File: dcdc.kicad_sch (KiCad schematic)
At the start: 25 parts, among them J10 Conn_01x01, J8 Conn_01x01, J9 Conn_01x01, T1 Transformer_SP_1S, U1 L78L33_SOT89, U2 TMP117, U3 LT3439

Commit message: asdf
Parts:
- added J11, J12: Conn_01x01, Connector_Wire:SolderWire-1sqmm_1x01_D1.4mm_OD3.9mm, symbol Connector_Generic:Conn_01x01
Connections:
- net 0Vout: now also J12.1 (Pin_1)
- net 12Vout: now also J11.1 (Pin_1)
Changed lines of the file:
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@@
+    (stroke (width 0) (type default) (color 0 0 0 0))
+  )
+  (wire (pts (xy 227.33 69.85) (xy 190.5 69.85))
     (stroke (width 0) (type default) (color 0 0 0 0))
   )
@@
     (stroke (width 0) (type default) (color 0 0 0 0))
   )
+  (wire (pts (xy 229.87 82.55) (xy 190.5 82.55))
+    (stroke (width 0) (type default) (color 0 0 0 0))
+  )
+  (wire (pts (xy 190.5 69.85) (xy 190.5 66.04))
+    (stroke (width 0) (type default) (color 0 0 0 0))
+  )
   (wire (pts (xy 116.84 101.6) (xy 127 101.6))
     (stroke (width 0) (type default) (color 0 0 0 0))
@@
   )
   (wire (pts (xy 49.53 134.62) (xy 49.53 137.16))
+    (stroke (width 0) (type default) (color 0 0 0 0))
+  )
+  (wire (pts (xy 190.5 82.55) (xy 190.5 74.93))
     (stroke (width 0) (type default) (color 0 0 0 0))
   )
@@
     (pin "1")
   )
+  (symbol (lib_id "Connector_Generic:Conn_01x01") (at 185.42 66.04 0) (mirror y) (unit 1)
+    (in_bom yes) (on_board yes) (fields_autoplaced)
+    (property "Reference" "J11" (id 0) (at 185.42 59.69 0))
+    (property "Value" "Conn_01x01" (id 1) (at 185.42 62.23 0))
+    (property "Footprint" "Connector_Wire:SolderWire-1sqmm_1x01_D1.4mm_OD3.9mm" (id 2) (at 185.42 66.04 0)
+      (effects (font (size 1.27 1.27)) hide)
+    )
+    (property "Datasheet" "~" (id 3) (at 185.42 66.04 0)
+      (effects (font (size 1.27 1.27)) hide)
+    )
+    (pin "1")
+  )
   (symbol (lib_id "Device:R") (at 59.69 140.97 0) (unit 1)
     (in_bom yes) (on_board yes) (fields_autoplaced)
@@
     (pin "2")
   )
+  (symbol (lib_id "Connector_Generic:Conn_01x01") (at 185.42 74.93 0) (mirror y) (unit 1)
+    (in_bom yes) (on_board yes) (fields_autoplaced)
+    (property "Reference" "J12" (id 0) (at 185.42 68.58 0))
+    (property "Value" "Conn_01x01" (id 1) (at 185.42 71.12 0))
+    (property "Footprint" "Connector_Wire:SolderWire-1sqmm_1x01_D1.4mm_OD3.9mm" (id 2) (at 185.42 74.93 0)
+      (effects (font (size 1.27 1.27)) hide)
+    )
+    (property "Datasheet" "~" (id 3) (at 185.42 74.93 0)
+      (effects (font (size 1.27 1.27)) hide)
+    )
+    (pin "1")
+  )
   (symbol (lib_id "Regulator_Switching:LT3439") (at 129.54 78.74 0) (unit 1)

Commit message: asdf
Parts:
- added H1, H2, H3, H4, H5, H6, H7, H8: MountingHole, MountingHole:MountingHole_4.3mm_M4, symbol Mechanical:MountingHole
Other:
- moved on the sheet: D1
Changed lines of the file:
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@@
     (pin "2")
+  )
+  (symbol (lib_id "Mechanical:MountingHole") (at 165.1 27.94 0) (unit 1)
+    (in_bom yes) (on_board yes) (fields_autoplaced)
+    (property "Reference" "H2" (id 0) (at 162.56 26.6699 0)
+      (effects (font (size 1.27 1.27)) (justify right))
+    )
+    (property "Value" "MountingHole" (id 1) (at 162.56 29.2099 0)
+      (effects (font (size 1.27 1.27)) (justify right))
+    )
+    (property "Footprint" "MountingHole:MountingHole_4.3mm_M4" (id 2) (at 165.1 27.94 0)
+      (effects (font (size 1.27 1.27)) hide)
+    )
+    (property "Datasheet" "~" (id 3) (at 165.1 27.94 0)
+      (effects (font (size 1.27 1.27)) hide)
+    )
   )
   (symbol (lib_id "power:GND") (at 77.47 180.34 0) (unit 1)
@@
     (pin "1")
     (pin "2")
+  )
+  (symbol (lib_id "Mechanical:MountingHole") (at 171.45 22.86 0) (unit 1)
+    (in_bom yes) (on_board yes) (fields_autoplaced)
+    (property "Reference" "H5" (id 0) (at 173.99 21.5899 0)
+      (effects (font (size 1.27 1.27)) (justify left))
+    )
+    (property "Value" "MountingHole" (id 1) (at 173.99 24.1299 0)
+      (effects (font (size 1.27 1.27)) (justify left))
+    )
+    (property "Footprint" "MountingHole:MountingHole_4.3mm_M4" (id 2) (at 171.45 22.86 0)
+      (effects (font (size 1.27 1.27)) hide)
+    )
+    (property "Datasheet" "~" (id 3) (at 171.45 22.86 0)
+      (effects (font (size 1.27 1.27)) hide)
+    )
   )
   (symbol (lib_id "Connector_Generic:Conn_01x01") (at 185.42 74.93 0) (mirror y) (unit 1)
@@
     (pin "2")
   )
+  (symbol (lib_id "Mechanical:MountingHole") (at 165.1 22.86 0) (unit 1)
+    (in_bom yes) (on_board yes) (fields_autoplaced)
+    (property "Reference" "H1" (id 0) (at 162.56 21.5899 0)
+      (effects (font (size 1.27 1.27)) (justify right))
+    )
+    (property "Value" "MountingHole" (id 1) (at 162.56 24.1299 0)
+      (effects (font (size 1.27 1.27)) (justify right))
+    )
+    (property "Footprint" "MountingHole:MountingHole_4.3mm_M4" (id 2) (at 165.1 22.86 0)
+      (effects (font (size 1.27 1.27)) hide)
+    )
+    (property "Datasheet" "~" (id 3) (at 165.1 22.86 0)
+      (effects (font (size 1.27 1.27)) hide)
+    )
+  )
   (symbol (lib_id "Regulator_Linear:L78L33_SOT89") (at 45.72 102.87 0) (unit 1)
     (in_bom yes) (on_board yes) (fields_autoplaced)
@@
     (pin "1")
   )
-  (symbol (lib_id "Device:LED") (at 233.68 36.83 180) (unit 1)
-    (in_bom yes) (on_board yes) (fields_autoplaced)
-    (property "Reference" "D1" (id 0) (at 235.2675 29.21 0))
-    (property "Value" "LED" (id 1) (at 235.2675 31.75 0))
-    (property "Footprint" "LED_SMD:LED_1206_3216Metric" (id 2) (at 233.68 36.83 0)
-      (effects (font (size 1.27 1.27)) hide)
-    )
-    (property "Datasheet" "~" (id 3) (at 233.68 36.83 0)
+  (symbol (lib_id "Device:LED") (at 233.68 31.75 180) (unit 1)
+    (in_bom yes) (on_board yes) (fields_autoplaced)
+    (property "Reference" "D1" (id 0) (at 235.2675 24.13 0))
+    (property "Value" "LED" (id 1) (at 235.2675 26.67 0))
+    (property "Footprint" "LED_SMD:LED_1206_3216Metric" (id 2) (at 233.68 31.75 0)
+      (effects (font (size 1.27 1.27)) hide)
+    )
+    (property "Datasheet" "~" (id 3) (at 233.68 31.75 0)
       (effects (font (size 1.27 1.27)) hide)
     )
@@
     (pin "2")
   )
+  (symbol (lib_id "Mechanical:MountingHole") (at 165.1 33.02 0) (unit 1)
+    (in_bom yes) (on_board yes) (fields_autoplaced)
+    (property "Reference" "H3" (id 0) (at 162.56 31.7499 0)
+      (effects (font (size 1.27 1.27)) (justify right))
+    )
+    (property "Value" "MountingHole" (id 1) (at 162.56 34.2899 0)
+      (effects (font (size 1.27 1.27)) (justify right))
+    )
+    (property "Footprint" "MountingHole:MountingHole_4.3mm_M4" (id 2) (at 165.1 33.02 0)
+      (effects (font (size 1.27 1.27)) hide)
+    )
+    (property "Datasheet" "~" (id 3) (at 165.1 33.02 0)
+      (effects (font (size 1.27 1.27)) hide)
+    )
+  )
+  (symbol (lib_id "Mechanical:MountingHole") (at 171.45 27.94 0) (unit 1)
+    (in_bom yes) (on_board yes) (fields_autoplaced)
+    (property "Reference" "H6" (id 0) (at 173.99 26.6699 0)
+      (effects (font (size 1.27 1.27)) (justify left))
+    )
+    (property "Value" "MountingHole" (id 1) (at 173.99 29.2099 0)
+      (effects (font (size 1.27 1.27)) (justify left))
+    )
+    (property "Footprint" "MountingHole:MountingHole_4.3mm_M4" (id 2) (at 171.45 27.94 0)
+      (effects (font (size 1.27 1.27)) hide)
+    )
+    (property "Datasheet" "~" (id 3) (at 171.45 27.94 0)
+      (effects (font (size 1.27 1.27)) hide)
+    )
+  )
   (symbol (lib_id "Jumper:Jumper_2_Open") (at 67.31 177.8 0) (mirror y) (unit 1)
     (in_bom yes) (on_board yes) (fields_autoplaced)
@@
     (pin "2")
   )
+  (symbol (lib_id "Mechanical:MountingHole") (at 171.45 38.1 0) (unit 1)
+    (in_bom yes) (on_board yes) (fields_autoplaced)
+    (property "Reference" "H8" (id 0) (at 173.99 36.8299 0)
+      (effects (font (size 1.27 1.27)) (justify left))
+    )
+    (property "Value" "MountingHole" (id 1) (at 173.99 39.3699 0)
+      (effects (font (size 1.27 1.27)) (justify left))
+    )
+    (property "Footprint" "MountingHole:MountingHole_4.3mm_M4" (id 2) (at 171.45 38.1 0)
+      (effects (font (size 1.27 1.27)) hide)
+    )
+    (property "Datasheet" "~" (id 3) (at 171.45 38.1 0)
+      (effects (font (size 1.27 1.27)) hide)
+    )
+  )
   (symbol (lib_id "Device:R") (at 49.53 140.97 0) (unit 1)
     (in_bom yes) (on_board yes) (fields_autoplaced)
@@
     (pin "1")
     (pin "2")
+  )
+  (symbol (lib_id "Mechanical:MountingHole") (at 165.1 38.1 0) (unit 1)
+    (in_bom yes) (on_board yes) (fields_autoplaced)
+    (property "Reference" "H4" (id 0) (at 162.56 36.8299 0)
+      (effects (font (size 1.27 1.27)) (justify right))
+    )
+    (property "Value" "MountingHole" (id 1) (at 162.56 39.3699 0)
+      (effects (font (size 1.27 1.27)) (justify right))
+    )
+    (property "Footprint" "MountingHole:MountingHole_4.3mm_M4" (id 2) (at 165.1 38.1 0)
+      (effects (font (size 1.27 1.27)) hide)
+    )
+    (property "Datasheet" "~" (id 3) (at 165.1 38.1 0)
+      (effects (font (size 1.27 1.27)) hide)
+    )
   )
   (symbol (lib_id "Device:R") (at 95.25 140.97 0) (unit 1)
@@
     (pin "1")
   )
+  (symbol (lib_id "Mechanical:MountingHole") (at 171.45 33.02 0) (unit 1)
+    (in_bom yes) (on_board yes) (fields_autoplaced)
+    (property "Reference" "H7" (id 0) (at 173.99 31.7499 0)
+      (effects (font (size 1.27 1.27)) (justify left))
+    )
+    (property "Value" "MountingHole" (id 1) (at 173.99 34.2899 0)
+      (effects (font (size 1.27 1.27)) (justify left))
+    )
+    (property "Footprint" "MountingHole:MountingHole_4.3mm_M4" (id 2) (at 171.45 33.02 0)
+      (effects (font (size 1.27 1.27)) hide)
+    )
+    (property "Datasheet" "~" (id 3) (at 171.45 33.02 0)
+      (effects (font (size 1.27 1.27)) hide)
+    )
+  )
   (symbol (lib_id "Device:C") (at 58.42 106.68 0) (unit 1)

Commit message: asdf
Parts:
- removed D2: LED, LED_SMD:LED_1206_3216Metric, symbol Device:LED
- added C? (x3): 22u, Capacitor_SMD:C_1206_3216Metric, symbol Device:C
- added C?: 100n, Capacitor_SMD:C_0805_2012Metric, symbol Device:C
- added D? (x4): D_Schottky, Diode_SMD:D_SOD-123F, symbol Device:D_Schottky
- added FL?: Choke_Schaffner_RN102-0.3-02-12M, Inductor_THT:Choke_Schaffner_RN102-04-14.0x14.0mm, symbol Filter:Choke_Schaffner_RN102-0.3-02-12M
- added R?: 5k, Resistor_SMD:R_0805_2012Metric, symbol Device:R
- added U?: LT3045xMSE, Package_SO:MSOP-12-1EP_3x4mm_P0.65mm_EP1.65x2.85mm, symbol Regulator_Linear:LT3045xMSE
- C3: footprint Capacitor_SMD:C_0805_2012Metric -> Capacitor_SMD:C_1206_3216Metric
- C6: value 100n -> 2.2n
- R4: value 5k -> 10k
- R5, R6: value 5k -> 16.9k
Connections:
- net +12V: now also C?.1, R?.1
- net 0Vout: no longer J12.1 (Pin_1)
- net 12Vout: no longer J11.1 (Pin_1)
- net GND: now also D1.1 (K), C?.2
- net at D1.2 (A): now also R?.2
- new net: C?.1, D?.1 (K), D?.1 (K), FL?.1
- new net: D?.1 (K), D?.2 (A), J11.1 (Pin_1)
- new net: C?.2, D?.2 (A), D?.2 (A), FL?.3
- new net: C?.1, C?.1, FL?.2
- new net: C?.2, C?.2, FL?.4
- new net: D?.1 (K), D?.2 (A), J12.1 (Pin_1)
- new net: U?.1 (IN), U?.2 (IN), U?.3 (IN), U?.4 (EN/UV)
- new net: U?.11 (OUT), U?.12 (OUT)
- new net: U?.13 (GND), U?.9 (GND)
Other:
- moved on the sheet: C1, C2, C3, C4, C5, C6, D1, H1, H2, H3, H4, H5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

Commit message: asdf
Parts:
- added C?: 100n, Capacitor_SMD:C_0805_2012Metric, symbol Device:C
- added R?: 121k, Resistor_SMD:R_0805_2012Metric, symbol Device:R
- added R?: 1k, Resistor_SMD:R_0805_2012Metric, symbol Device:R
- gave numbers to parts that had none: 11
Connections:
- net at C13.1, C14.1, FL1.2: now also U6.1 (IN), U6.2 (IN), U6.3 (IN), U6.4 (EN/UV)
- net at C13.2, C14.2, FL1.4: now also U6.13 (GND), U6.9 (GND), C?.2, R?.2, R?.2
- net at U6.10 (OUTS): now also U6.11 (OUT), U6.12 (OUT)
- net at U6.6 (ILIM): now also R?.1
- net at U6.8 (SET): now also C?.1, R?.1
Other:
- moved on the sheet: C12, C13, C14, D2, D5, D6, D7, FL1, J11, J12, J8, T1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

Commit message: asdf
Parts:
- removed C13: 22u, Capacitor_SMD:C_1206_3216Metric, symbol Device:C
- removed FL1: Choke_Schaffner_RN102-0.3-02-12M, Inductor_THT:Choke_Schaffner_RN102-04-14.0x14.0mm, symbol Filter:Choke_Schaffner_RN102-0.3-02-12M
- gave numbers to parts that had none: 3
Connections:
- net at C12.1, D2.1 (K), D6.1 (K): now also C14.1, U6.1 (IN), U6.2 (IN), U6.3 (IN), U6.4 (EN/UV)
- net at C12.2, D5.2 (A), D7.2 (A): now also C14.2, C15.2, R11.2, R12.2, U6.13 (GND), U6.9 (GND)
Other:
- moved on the sheet: C14, C15, R11, R12, U6

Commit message: asdf
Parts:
- added D8: LED, LED_SMD:LED_1206_3216Metric, symbol Device:LED
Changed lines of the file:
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@@
+    (pin "2")
+  )
+  (symbol (lib_id "Device:LED") (at 83.82 27.94 180) (unit 1)
+    (in_bom yes) (on_board yes) (fields_autoplaced)
+    (property "Reference" "D8" (id 0) (at 85.4075 20.32 0))
+    (property "Value" "LED" (id 1) (at 85.4075 22.86 0))
+    (property "Footprint" "LED_SMD:LED_1206_3216Metric" (id 2) (at 83.82 27.94 0)
+      (effects (font (size 1.27 1.27)) hide)
+    )
+    (property "Datasheet" "~" (id 3) (at 83.82 27.94 0)
+      (effects (font (size 1.27 1.27)) hide)
+    )
+    (pin "1")
     (pin "2")
   )

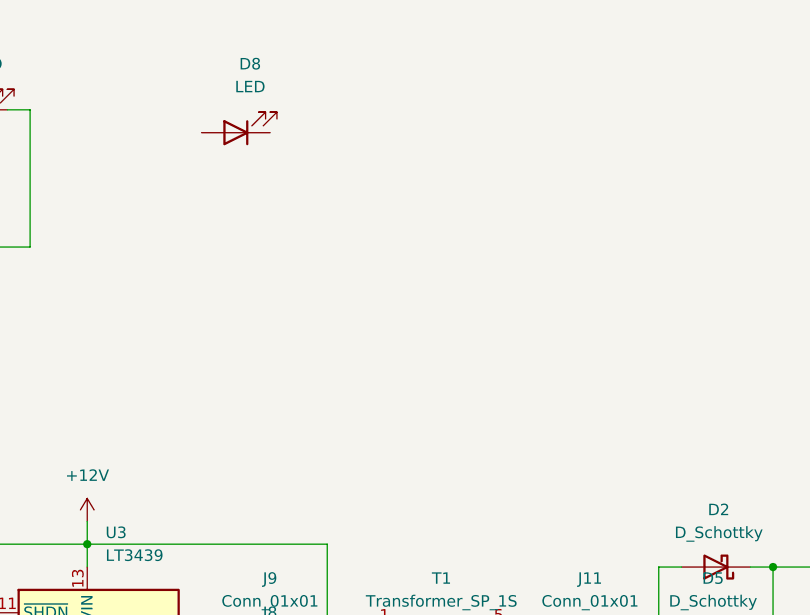
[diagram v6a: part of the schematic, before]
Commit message: added i2c temperature sensor and eeprom
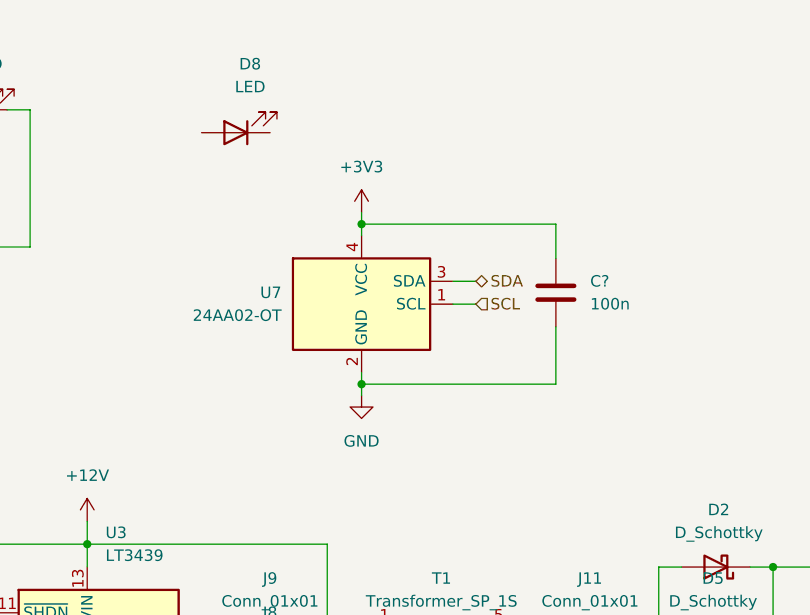
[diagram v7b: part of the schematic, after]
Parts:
- added C?: 100n, Capacitor_SMD:C_0805_2012Metric, symbol Device:C
- added U7: 24AA02-OT, Package_TO_SOT_SMD:SOT-23-5, symbol Memory_EEPROM:24AA02-OT
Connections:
- net +3V3: now also C?.1, U7.4 (VCC)
- net GND: now also C?.2, U7.2 (GND)
- net SCL: now also U7.1 (SCL)
- net SDA: now also U7.3 (SDA)
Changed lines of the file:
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@@
   (junction (at 146.05 100.33) (diameter 0) (color 0 0 0 0)
   )
+  (junction (at 97.79 38.1) (diameter 0) (color 0 0 0 0)
+  )
   (junction (at 48.26 111.76) (diameter 0) (color 0 0 0 0)
   )
@@
   (junction (at 54.61 111.76) (diameter 0) (color 0 0 0 0)
   )
+  (junction (at 97.79 55.88) (diameter 0) (color 0 0 0 0)
+  )
   (wire (pts (xy 187.96 76.2) (xy 190.5 76.2))
     (stroke (width 0) (type default) (color 0 0 0 0))
@@
     (stroke (width 0) (type default) (color 0 0 0 0))
   )
+  (wire (pts (xy 107.95 46.99) (xy 110.49 46.99))
+    (stroke (width 0) (type default) (color 0 0 0 0))
+  )
+  (wire (pts (xy 97.79 55.88) (xy 97.79 57.15))
+    (stroke (width 0) (type default) (color 0 0 0 0))
+  )
   (wire (pts (xy 143.51 76.2) (xy 143.51 91.44))
     (stroke (width 0) (type default) (color 0 0 0 0))
@@
     (stroke (width 0) (type default) (color 0 0 0 0))
   )
+  (wire (pts (xy 119.38 55.88) (xy 119.38 49.53))
+    (stroke (width 0) (type default) (color 0 0 0 0))
+  )
   (wire (pts (xy 152.4 140.97) (xy 152.4 154.94))
     (stroke (width 0) (type default) (color 0 0 0 0))
@@
     (stroke (width 0) (type default) (color 0 0 0 0))
   )
+  (wire (pts (xy 119.38 38.1) (xy 119.38 41.91))
+    (stroke (width 0) (type default) (color 0 0 0 0))
+  )
   (wire (pts (xy 25.4 111.76) (xy 25.4 109.22))
     (stroke (width 0) (type default) (color 0 0 0 0))
@@
     (stroke (width 0) (type default) (color 0 0 0 0))
   )
+  (wire (pts (xy 97.79 38.1) (xy 119.38 38.1))
+    (stroke (width 0) (type default) (color 0 0 0 0))
+  )
   (wire (pts (xy 147.32 140.97) (xy 152.4 140.97))
     (stroke (width 0) (type default) (color 0 0 0 0))
@@
     (stroke (width 0) (type default) (color 0 0 0 0))
   )
+  (wire (pts (xy 107.95 44.45) (xy 110.49 44.45))
+    (stroke (width 0) (type default) (color 0 0 0 0))
+  )
   (wire (pts (xy 69.85 104.14) (xy 69.85 111.76))
     (stroke (width 0) (type default) (color 0 0 0 0))
@@
     (stroke (width 0) (type default) (color 0 0 0 0))
   )
+  (wire (pts (xy 97.79 55.88) (xy 119.38 55.88))
+    (stroke (width 0) (type default) (color 0 0 0 0))
+  )
   (wire (pts (xy 36.83 109.22) (xy 36.83 111.76))
     (stroke (width 0) (type default) (color 0 0 0 0))
@@
     (stroke (width 0) (type default) (color 0 0 0 0))
   )
+  (wire (pts (xy 97.79 36.83) (xy 97.79 38.1))
+    (stroke (width 0) (type default) (color 0 0 0 0))
+  )
+  (wire (pts (xy 97.79 54.61) (xy 97.79 55.88))
+    (stroke (width 0) (type default) (color 0 0 0 0))
+  )
   (wire (pts (xy 57.15 81.28) (xy 54.61 81.28))
+    (stroke (width 0) (type default) (color 0 0 0 0))
+  )
+  (wire (pts (xy 97.79 38.1) (xy 97.79 39.37))
     (stroke (width 0) (type default) (color 0 0 0 0))
   )
@@
     (effects (font (size 1.27 1.27)) (justify right))
   )
+  (hierarchical_label "SDA" (shape bidirectional) (at 110.49 44.45 0)
+    (effects (font (size 1.27 1.27)) (justify left))
+  )
   (hierarchical_label "sync" (shape input) (at 34.29 93.98 180)
     (effects (font (size 1.27 1.27)) (justify right))
@@
   (hierarchical_label "Vin+" (shape input) (at 25.4 25.4 180)
     (effects (font (size 1.27 1.27)) (justify right))
+  )
+  (hierarchical_label "SCL" (shape input) (at 110.49 46.99 0)
+    (effects (font (size 1.27 1.27)) (justify left))
   )
   (symbol (lib_id "Connector_Generic:Conn_01x01") (at 87.63 87.63 0) (mirror y) (unit 1)
@@
     )
     (pin "1")
+  )
+  (symbol (lib_id "Memory_EEPROM:24AA02-OT") (at 97.79 46.99 0) (unit 1)
+    (in_bom yes) (on_board yes) (fields_autoplaced)
+    (property "Reference" "U7" (id 0) (at 88.9 45.7199 0)
+      (effects (font (size 1.27 1.27)) (justify right))
+    )
+    (property "Value" "24AA02-OT" (id 1) (at 88.9 48.2599 0)
+      (effects (font (size 1.27 1.27)) (justify right))
+    )
+    (property "Footprint" "Package_TO_SOT_SMD:SOT-23-5" (id 2) (at 97.79 46.99 0)
+      (effects (font (size 1.27 1.27)) hide)
+    )
+    (property "Datasheet" "http://ww1.microchip.com/downloads/en/DeviceDoc/21709J.pdf" (id 3) (at 97.79 46.99 0)
+      (effects (font (size 1.27 1.27)) hide)
+    )
+    (pin "1")
+    (pin "2")
+    (pin "3")
+    (pin "4")
+    (pin "5")
   )
   (symbol (lib_id "Device:R") (at 54.61 105.41 0) (unit 1)
@@
     (pin "2")
   )
+  (symbol (lib_id "power:+3V3") (at 97.79 36.83 0) (unit 1)
+    (in_bom yes) (on_board yes) (fields_autoplaced)
+    (property "Reference" "#PWR0111" (id 0) (at 97.79 40.64 0)
+      (effects (font (size 1.27 1.27)) hide)
+    )
+    (property "Value" "+3V3" (id 1) (at 97.79 31.75 0))
+    (property "Footprint" "" (id 2) (at 97.79 36.83 0)
+      (effects (font (size 1.27 1.27)) hide)
+    )
+    (property "Datasheet" "" (id 3) (at 97.79 36.83 0)
+      (effects (font (size 1.27 1.27)) hide)
+    )
+    (pin "1")
+  )
   (symbol (lib_id "Device:C_Polarized") (at 27.94 33.02 0) (unit 1)
     (in_bom yes) (on_board yes) (fields_autoplaced)
@@
     (pin "1")
     (pin "2")
+  )
+  (symbol (lib_id "power:GND") (at 97.79 57.15 0) (unit 1)
+    (in_bom yes) (on_board yes) (fields_autoplaced)
+    (property "Reference" "#PWR0110" (id 0) (at 97.79 63.5 0)
+      (effects (font (size 1.27 1.27)) hide)
+    )
+    (property "Value" "GND" (id 1) (at 97.79 62.23 0))
+    (property "Footprint" "" (id 2) (at 97.79 57.15 0)
+      (effects (font (size 1.27 1.27)) hide)
+    )
+    (property "Datasheet" "" (id 3) (at 97.79 57.15 0)
+      (effects (font (size 1.27 1.27)) hide)
+    )
+    (pin "1")
   )
   (symbol (lib_id "Regulator_Linear:L78L33_SOT89") (at 45.72 153.67 0) (unit 1)
@@
       (effects (font (size 1.27 1.27)) hide)
     )
+    (pin "1")
+    (pin "2")
+  )
+  (symbol (lib_id "Device:C") (at 119.38 45.72 0) (unit 1)
+    (in_bom yes) (on_board yes) (fields_autoplaced)
+    (property "Reference" "C?" (id 0) (at 123.19 44.4499 0)
+      (effects (font (size 1.27 1.27)) (justify left))
+    )
+    (property "Value" "100n" (id 1) (at 123.19 46.9899 0)
+      (effects (font (size 1.27 1.27)) (justify left))
+    )
+    (property "Footprint" "Capacitor_SMD:C_0805_2012Metric" (id 2) (at 120.3452 49.53 0)
+      (effects (font (size 1.27 1.27)) hide)
+    )
+    (property "Datasheet" "~" (id 3) (at 119.38 45.72 0)
+      (effects (font (size 1.27 1.27)) hide)
+    )

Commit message: asas
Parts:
- added C17: 22u, Capacitor_SMD:C_1206_3216Metric, symbol Device:C
- added Q2: MMBT3904, Package_TO_SOT_SMD:SOT-23, symbol Transistor_BJT:MMBT3904
- added R19: 5k, Resistor_SMD:R_0805_2012Metric, symbol Device:R
- added R20: 200k, Resistor_SMD:R_0805_2012Metric, symbol Device:R
- added R21: 1.8M, Resistor_SMD:R_0805_2012Metric, symbol Device:R
- added R22: 49.9k, Resistor_SMD:R_0805_2012Metric, symbol Device:R
- gave numbers to parts that had none: 1
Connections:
- net 0Vout: now also C12.2, C14.2, C15.2, D5.2 (A), D7.2 (A), D8.1 (K), R11.2, R12.2, U6.13 (GND), U6.9 (GND), C17.2, R22.2
- net 12Vout: now also U6.10 (OUTS), U6.11 (OUT), U6.12 (OUT), C17.1, R21.1
- net at C12.1, C14.1, D2.1 (K)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: now also Q2.3 (C), R20.2
- net at D8.2 (A): now also R19.2
- net PG: now reaches U6.5 (PG)
- net PG: now also Q2.1 (B), R20.1
- net at U6.7 (PGFB): now also R21.2, R22.1
- new net status: Q2.2 (E), R19.1
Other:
- moved on the sheet: C12, C14, C15, D2, D7, D8, R11, R12, T1, U6
